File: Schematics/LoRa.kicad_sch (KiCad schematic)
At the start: 1 part, among them J4 Conn_Coaxial_Small

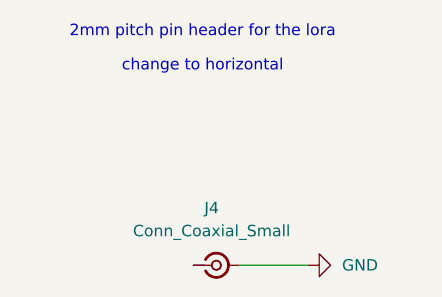
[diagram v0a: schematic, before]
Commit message: added LCSC numbers and footprint values, need to connect schemeatic pins, then can start layout
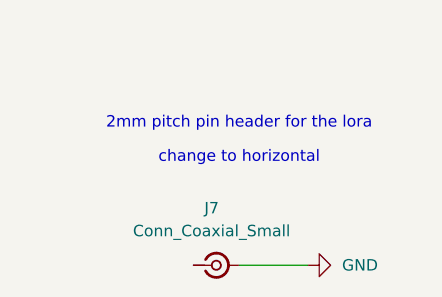
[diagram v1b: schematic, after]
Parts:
- J7: renamed from J4; LCSC Part (none) -> C3172376
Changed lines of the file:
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@@
 	(text "2mm pitch pin header for the lora\n"
 		(exclude_from_sim no)
-		(at 119.126 65.532 0)
+		(at 123.19 75.692 0)
 		(effects
 			(font
@@
 	(text "change to horizontal\n"
 		(exclude_from_sim no)
-		(at 119.126 69.342 0)
+		(at 123.19 79.502 0)
 		(effects
 			(font
@@
 		(dnp no)
 		(fields_autoplaced yes)
-		(property "Reference" "#PWR014"
+		(property "Reference" "#PWR057"
 			(at 137.16 91.44 0)
 			(effects
@@
 			(project "flightcomputer2"
 				(path "/6cb3dda3-5fe8-4715-b831-354360aa3199/97ae08f8-7044-40a2-9385-378b47d6b9a1"
-					(reference "#PWR014")
+					(reference "#PWR057")
 					(unit 1)
 				)
@@
 		(dnp no)
 		(fields_autoplaced yes)
-		(property "Reference" "J4"
+		(property "Reference" "J7"
 			(at 120.1304 85.09 0)
 			(effects
@@
 			)
 		)
+		(property "Sim.Device" ""
+			(at 120.65 91.44 0)
+			(effects
+				(font
+					(size 1.27 1.27)
+				)
+				(hide yes)
+			)
+		)
+		(property "Sim.Type" ""
+			(at 120.65 91.44 0)
+			(effects
+				(font
+					(size 1.27 1.27)
+				)
+				(hide yes)
+			)
+		)
+		(property "LCSC Part" "C3172376"
+			(at 120.65 91.44 0)
+			(effects
+				(font
+					(size 1.27 1.27)
+				)
+				(hide yes)
+			)
+		)
 		(pin "1"
 		)
@@
 			(project "flightcomputer2"
 				(path "/6cb3dda3-5fe8-4715-b831-354360aa3199/97ae08f8-7044-40a2-9385-378b47d6b9a1"
-					(reference "J4")
+					(reference "J7")
 					(unit 1)
 				)

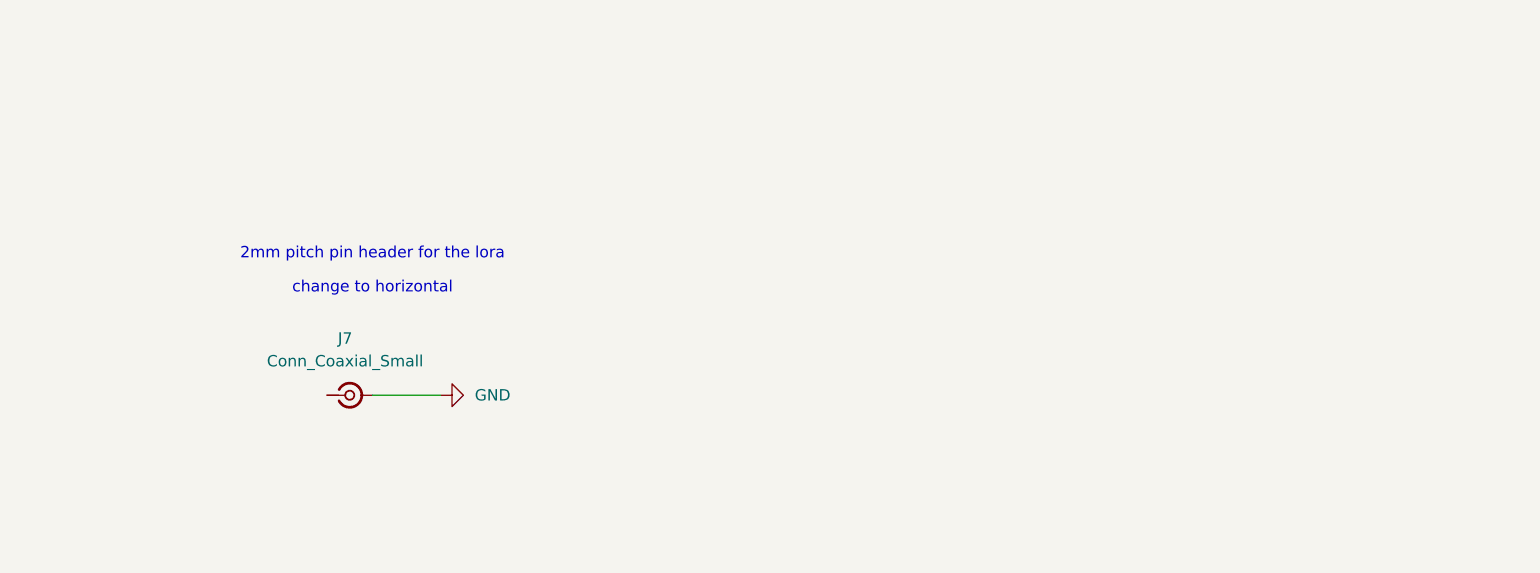
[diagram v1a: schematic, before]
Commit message: started lora schematic all pcb parts should be included
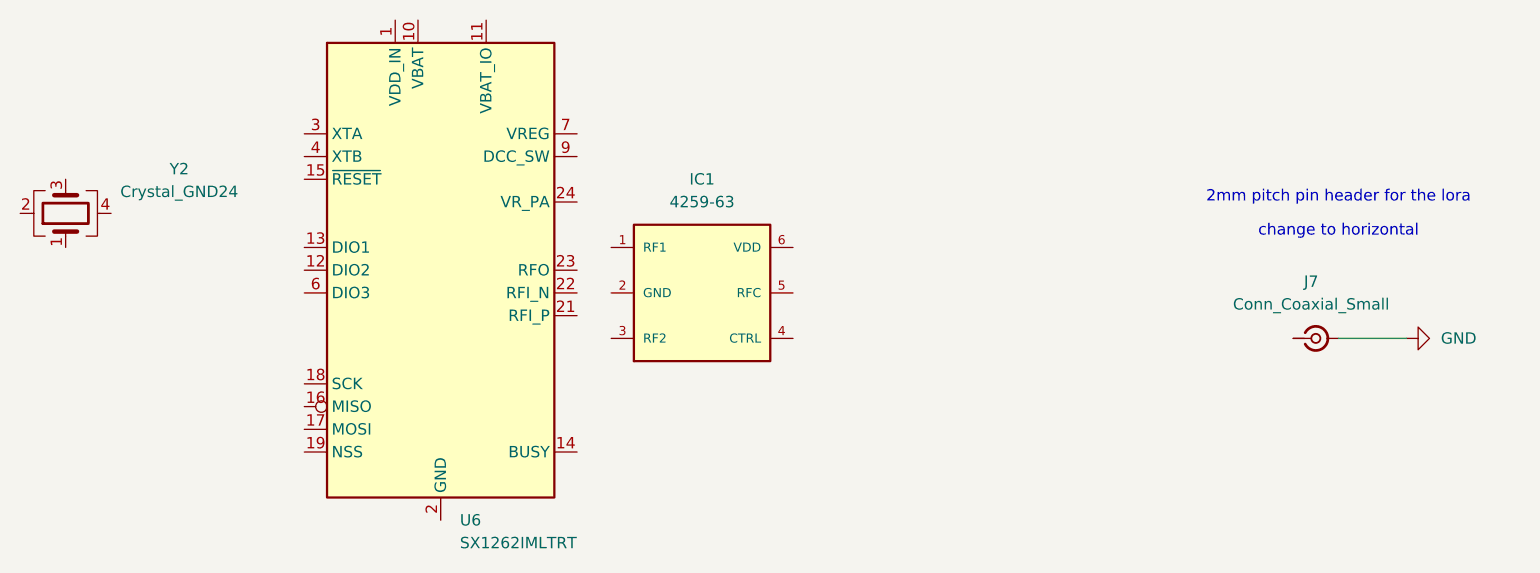
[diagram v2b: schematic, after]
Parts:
- added IC1: 4259-63, 4259-63:SC-70-6, symbol 4259-63:4259-63
- added U6: SX1262IMLTRT, Package_DFN_QFN:QFN-24-1EP_4x4mm_P0.5mm_EP2.6x2.6mm, symbol RF:SX1262IMLTRT
- added Y2: Crystal_GND24, Crystal:Crystal_SMD_2016-4Pin_2.0x1.6mm, symbol Device:Crystal_GND24
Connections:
- new net: U6.2 (GND), U6.20 (GND), U6.25 (GND), U6.5 (GND), U6.8 (GND)
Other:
- moved on the sheet: J7

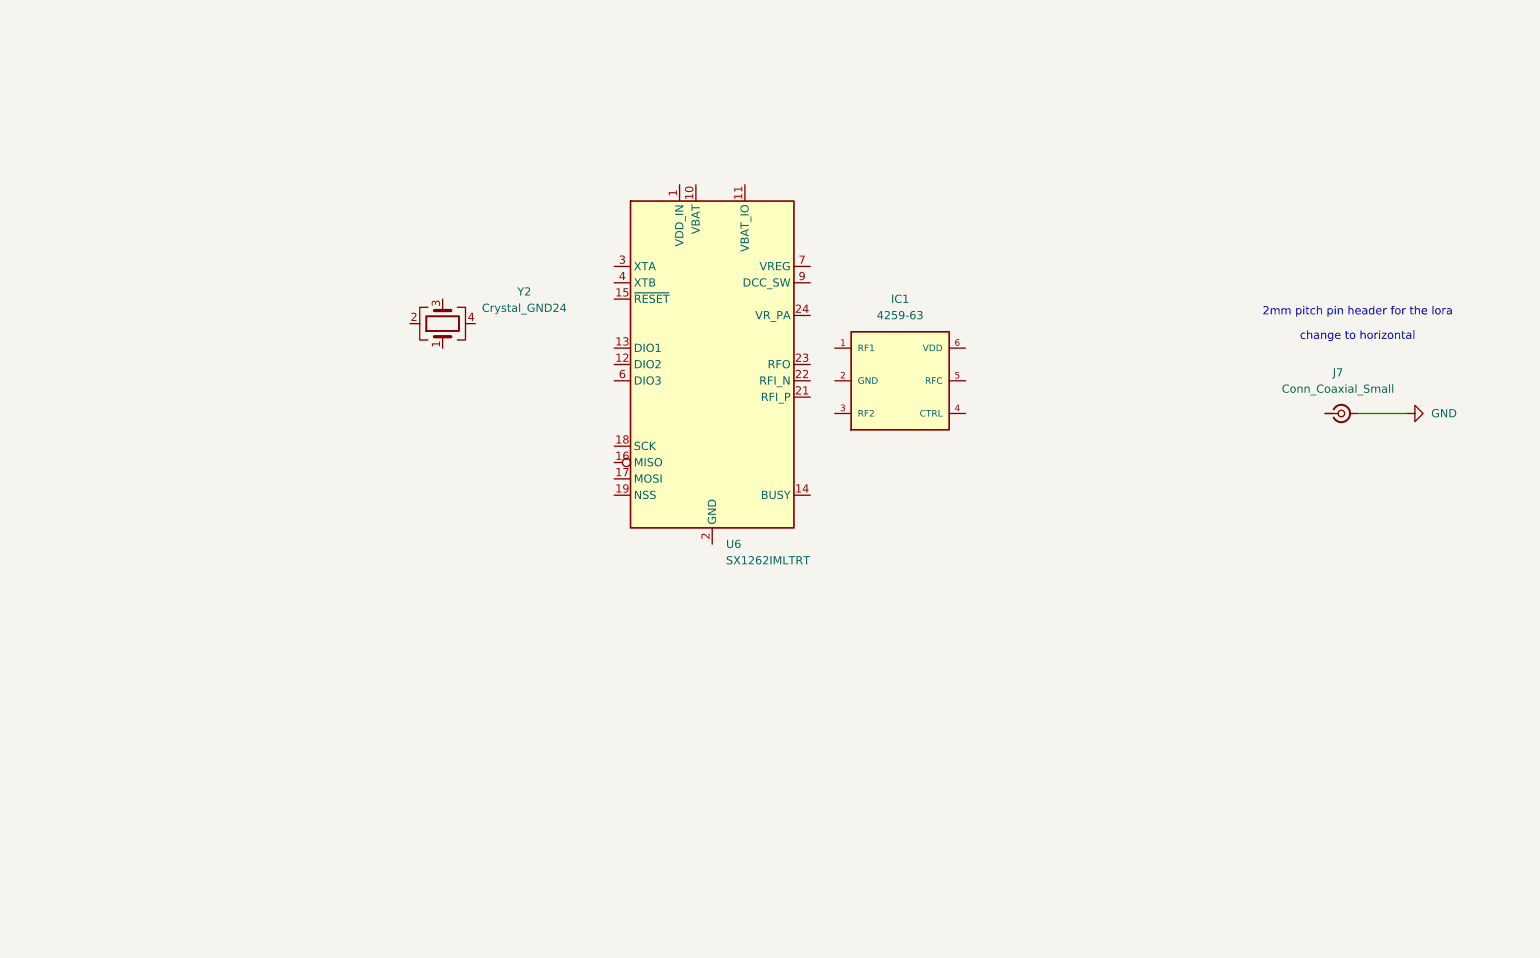
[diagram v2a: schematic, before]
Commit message: added sx1262x according to refrence
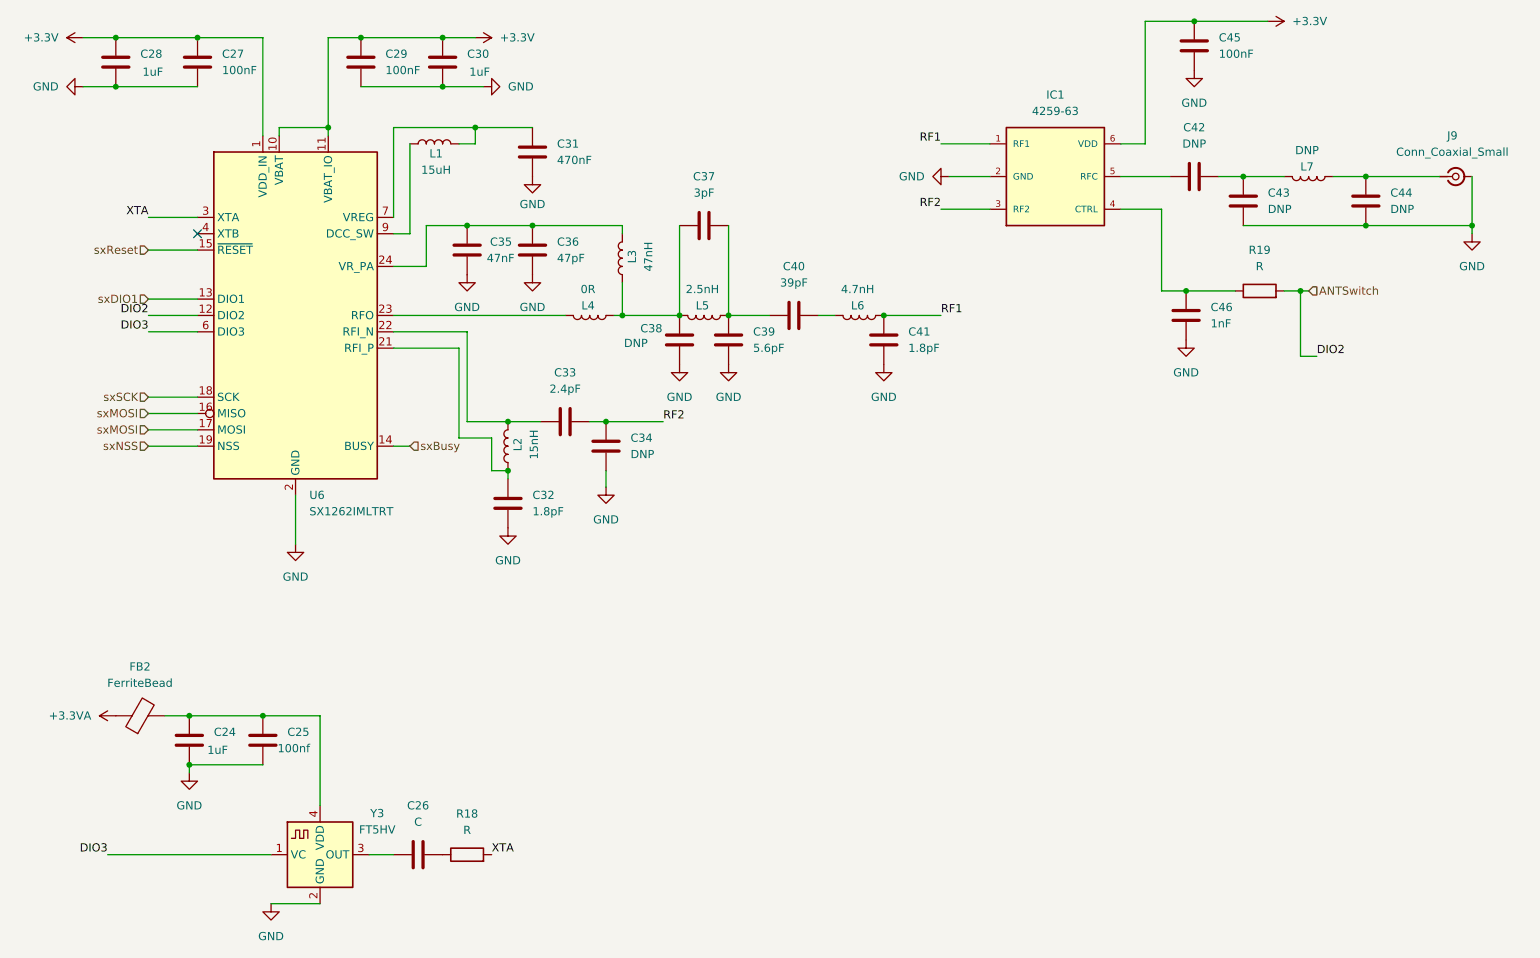
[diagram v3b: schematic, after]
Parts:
- removed J7: Conn_Coaxial_Small, Connector_Coaxial:SMA_Amphenol_132291_Vertical, symbol Connector:Conn_Coaxial_Small
- removed Y2: Crystal_GND24, Crystal:Crystal_SMD_2016-4Pin_2.0x1.6mm, symbol Device:Crystal_GND24
- added C24, C28, C30: 1uF, symbol Device:C
- added C25: 100nf, symbol Device:C
- added C26: C, symbol Device:C
- added C27, C29, C45: 100nF, symbol Device:C
- added C31: 470nF, symbol Device:C
- added C32, C41: 1.8pF, symbol Device:C
- added C33: 2.4pF, symbol Device:C
- added C34, C38, C42, C43, C44: DNP, symbol Device:C
- added C35: 47nF, symbol Device:C
- added C36: 47pF, symbol Device:C
- added C37: 3pF, symbol Device:C
- added C39: 5.6pF, symbol Device:C
- added C40: 39pF, symbol Device:C
- added C46: 1nF, symbol Device:C
- added FB2: FerriteBead, symbol Device:FerriteBead
- added J9: Conn_Coaxial_Small, Connector_Coaxial:SMA_Amphenol_132291_Vertical, symbol Connector:Conn_Coaxial_Small
- added L1: 15uH, symbol Device:L
- added L2: 15nH, symbol Device:L
- added L3: 47nH, symbol Device:L
- added L4: 0R, symbol Device:L
- added L5: 2.5nH, symbol Device:L
- added L6: 4.7nH, symbol Device:L
- added L7: DNP, symbol Device:L
- added R18, R19: R, symbol Device:R
- added Y3: FT5HV, Oscillator:Oscillator_SMD_Fox_FT5H_5.0x3.2mm, symbol Oscillator:FT5HV
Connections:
- net GND: now also IC1.2 (GND), U6.2 (GND), U6.20 (GND), U6.25 (GND), U6.5 (GND), U6.8 (GND), C24.2, C25.2, C27.2, C28.2, C29.2, C30.2, C31.2, C32.2, C34.2, C35.2, C36.2, C38.2, C39.2, C41.1, C43.1, C44.1, C45.1, C46.1, J9.2 (Ext), Y3.2 (GND)
- net +3.3V: now reaches U6.1 (VDD_IN)
- net +3.3V: now also IC1.6 (VDD), U6.10 (VBAT), U6.11 (VBAT_IO), C27.1, C28.1, C29.1, C30.1, C45.2
- net ANTSwitch: now reaches U6.12 (DIO2)
- net ANTSwitch: now also R19.2
- net sxDIO1: now reaches U6.13 (DIO1)
- net sxBusy: now reaches U6.14 (BUSY)
- net sxReset: now reaches U6.15 (~{RESET})
- net sxMOSI: now reaches U6.16 (MISO)
- net sxMOSI: now also U6.17 (MOSI)
- net sxSCK: now reaches U6.18 (SCK)
- net sxNSS: now reaches U6.19 (NSS)
- net at U6.21 (RFI_P): now also C32.1, L2.1
- net at U6.22 (RFI_N): now also C33.1, L2.2
- net at U6.23 (RFO): now also L4.2
- net at U6.24 (VR_PA): now also C35.1, C36.1, L3.2
- net XTA: now reaches U6.3 (XTA)
- net XTA: now also R18.2
- net DIO3: now reaches U6.6 (DIO3)
- net DIO3: now also Y3.1 (VC)
- net at U6.7 (VREG): now also C31.1, L1.2
- net at U6.9 (DCC_SW): now also L1.1
- net RF1: now reaches IC1.1 (RF1)
- net RF1: now also C41.2, L6.1
- net RF2: now reaches IC1.3 (RF2)
- net RF2: now also C33.2, C34.1
- net at IC1.4 (CTRL): now also C46.2, R19.1
- net at IC1.5 (RFC): now also C42.1
- new net: C44.2, J9.1 (In), L7.1
- new net: C26.1, Y3.3 (OUT)
- new net: C26.2, R18.1
- new net: C37.1, C38.1, L3.1, L4.1, L5.2
- new net: C40.2, L6.2
- new net: C24.1, C25.1, FB2.2, Y3.4 (VDD)
- new net: C37.2, C39.1, C40.1, L5.1
- new net: C42.2, C43.2, L7.2
- new net +3.3VA: FB2.1
- no-connect marks 0 -> 1
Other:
- note removed: "2mm pitch pin header for the lora"
- note removed: "change to horizontal"
- moved on the sheet: IC1, U6

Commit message: fixed symbols and added diodes to power input before ldo
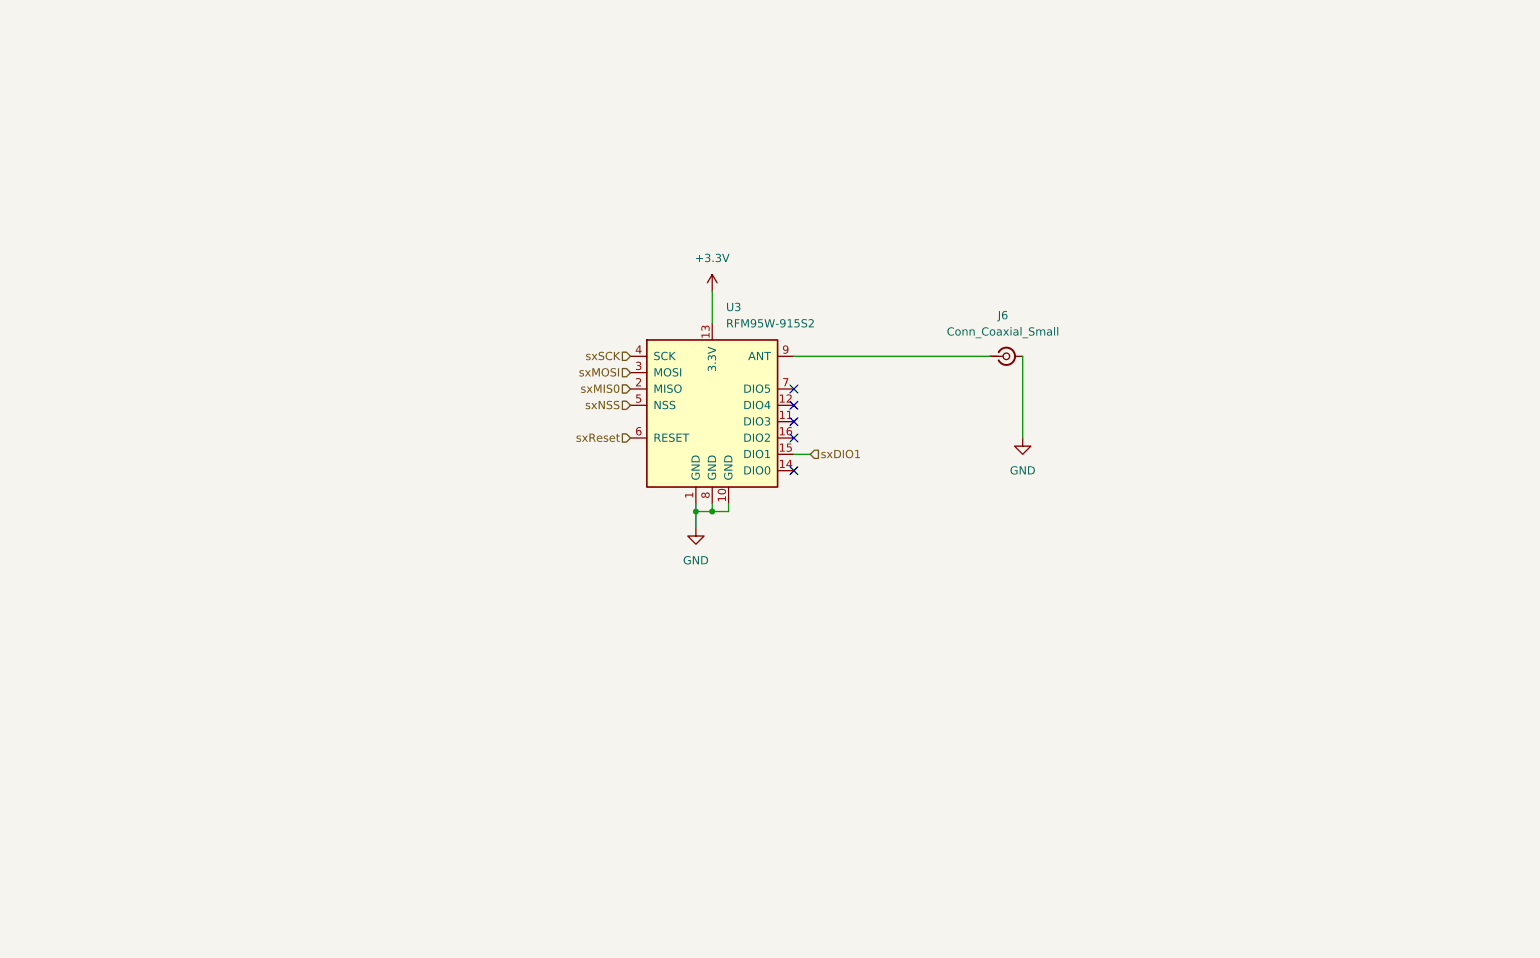
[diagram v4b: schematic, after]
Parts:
- removed C24, C28, C30: 1uF, symbol Device:C
- removed C25: 100nf, symbol Device:C
- removed C26: C, symbol Device:C
- removed C27, C29, C45: 100nF, symbol Device:C
- removed C31: 470nF, symbol Device:C
- removed C32, C41: 1.8pF, symbol Device:C
- removed C33: 2.4pF, symbol Device:C
- removed C34, C38, C42, C43, C44: DNP, symbol Device:C
- removed C35: 47nF, symbol Device:C
- removed C36: 47pF, symbol Device:C
- removed C37: 3pF, symbol Device:C
- removed C39: 5.6pF, symbol Device:C
- removed C40: 39pF, symbol Device:C
- removed C46: 1nF, symbol Device:C
- removed FB2: FerriteBead, symbol Device:FerriteBead
- removed IC1: 4259-63, 4259-63:SC-70-6, symbol 4259-63:4259-63
- removed J9: Conn_Coaxial_Small, Connector_Coaxial:SMA_Amphenol_132291_Vertical, symbol Connector:Conn_Coaxial_Small
- removed L1: 15uH, symbol Device:L
- removed L2: 15nH, symbol Device:L
- removed L3: 47nH, symbol Device:L
- removed L4: 0R, symbol Device:L
- removed L5: 2.5nH, symbol Device:L
- removed L6: 4.7nH, symbol Device:L
- removed L7: DNP, symbol Device:L
- removed R18, R19: R, symbol Device:R
- removed U6: SX1262IMLTRT, Package_DFN_QFN:QFN-24-1EP_4x4mm_P0.5mm_EP2.6x2.6mm, symbol RF:SX1262IMLTRT
- removed Y3: FT5HV, Oscillator:Oscillator_SMD_Fox_FT5H_5.0x3.2mm, symbol Oscillator:FT5HV
- added J6: Conn_Coaxial_Small, Connector_Coaxial:SMA_Amphenol_132291_Vertical, symbol Connector:Conn_Coaxial_Small
- added U3: RFM95W-915S2, symbol RF_Module:RFM95W-915S2
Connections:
- net +3.3V: now also U3.13 (3.3V)
- net GND: now also J6.2 (Ext), U3.1 (GND), U3.10 (GND), U3.8 (GND)
- net sxDIO1: now also U3.15 (DIO1)
- net sxMOSI: now also U3.3 (MOSI)
- net sxNSS: now also U3.5 (NSS)
- net sxReset: now also U3.6 (RESET)
- net sxSCK: now also U3.4 (SCK)
- new net: J6.1 (In), U3.9 (ANT)
- new net sxMIS0: U3.2 (MISO)
- no-connect marks 1 -> 5
